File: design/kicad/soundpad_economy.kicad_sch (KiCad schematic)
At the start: 9 parts

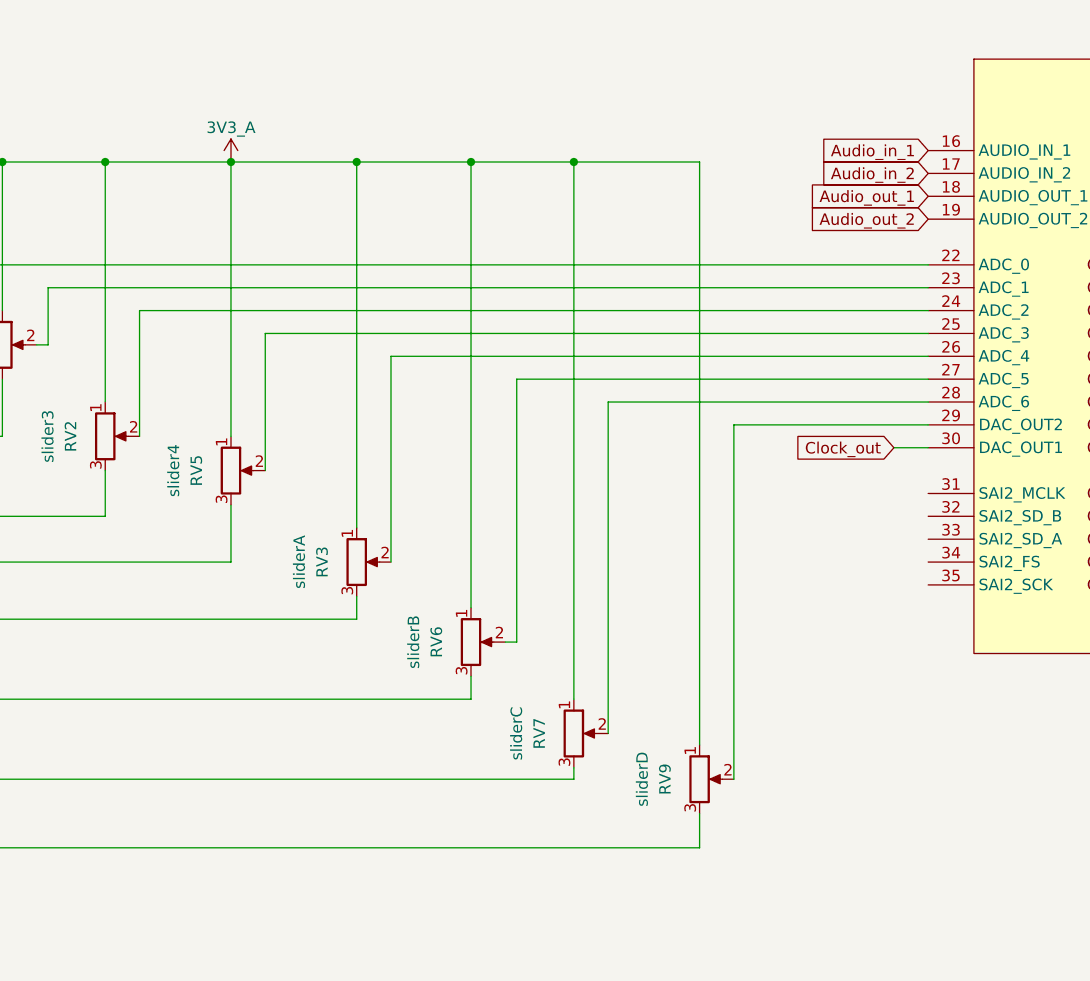
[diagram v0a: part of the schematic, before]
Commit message: PCB moves analog signals to back plane
so that ground plane inbetween them and digital signals. Also moves digital signals away from back plane and instead weaves them between the two top planes.
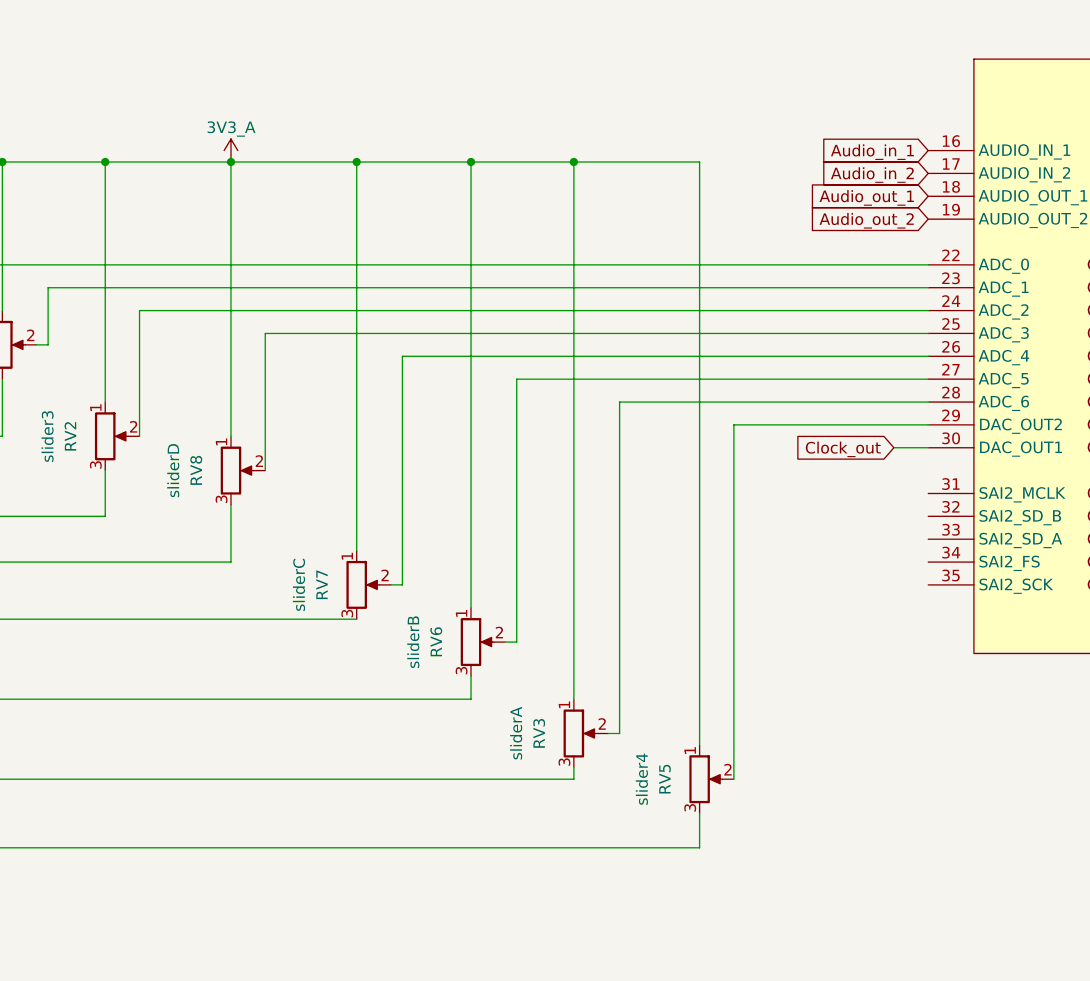
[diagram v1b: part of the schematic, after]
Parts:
- removed RV9: sliderD, Potentiometer_THT:Potentiometer_Bourns_PTA4543_Single_Slide, symbol Device:R_Potentiometer
- added RV8: sliderD, Potentiometer_THT:Potentiometer_Bourns_PTA4543_Single_Slide, symbol Device:R_Potentiometer
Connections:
- net 3V3_A: now also RV8.1
- net GND: now also RV8.3
- net at A1.25 (ADC_3): now also RV8.2; no longer RV5.2
- net at A1.29 (DAC_OUT2): now also RV5.2
- net at RV7.2: now also A1.26 (ADC_4); no longer A1.28 (ADC_6)
- net at RV3.2: now also A1.28 (ADC_6); no longer A1.26 (ADC_4)
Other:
- moved on the sheet: RV3, RV7
